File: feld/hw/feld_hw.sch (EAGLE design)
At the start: 23 parts, among them X1 PINH2X3N

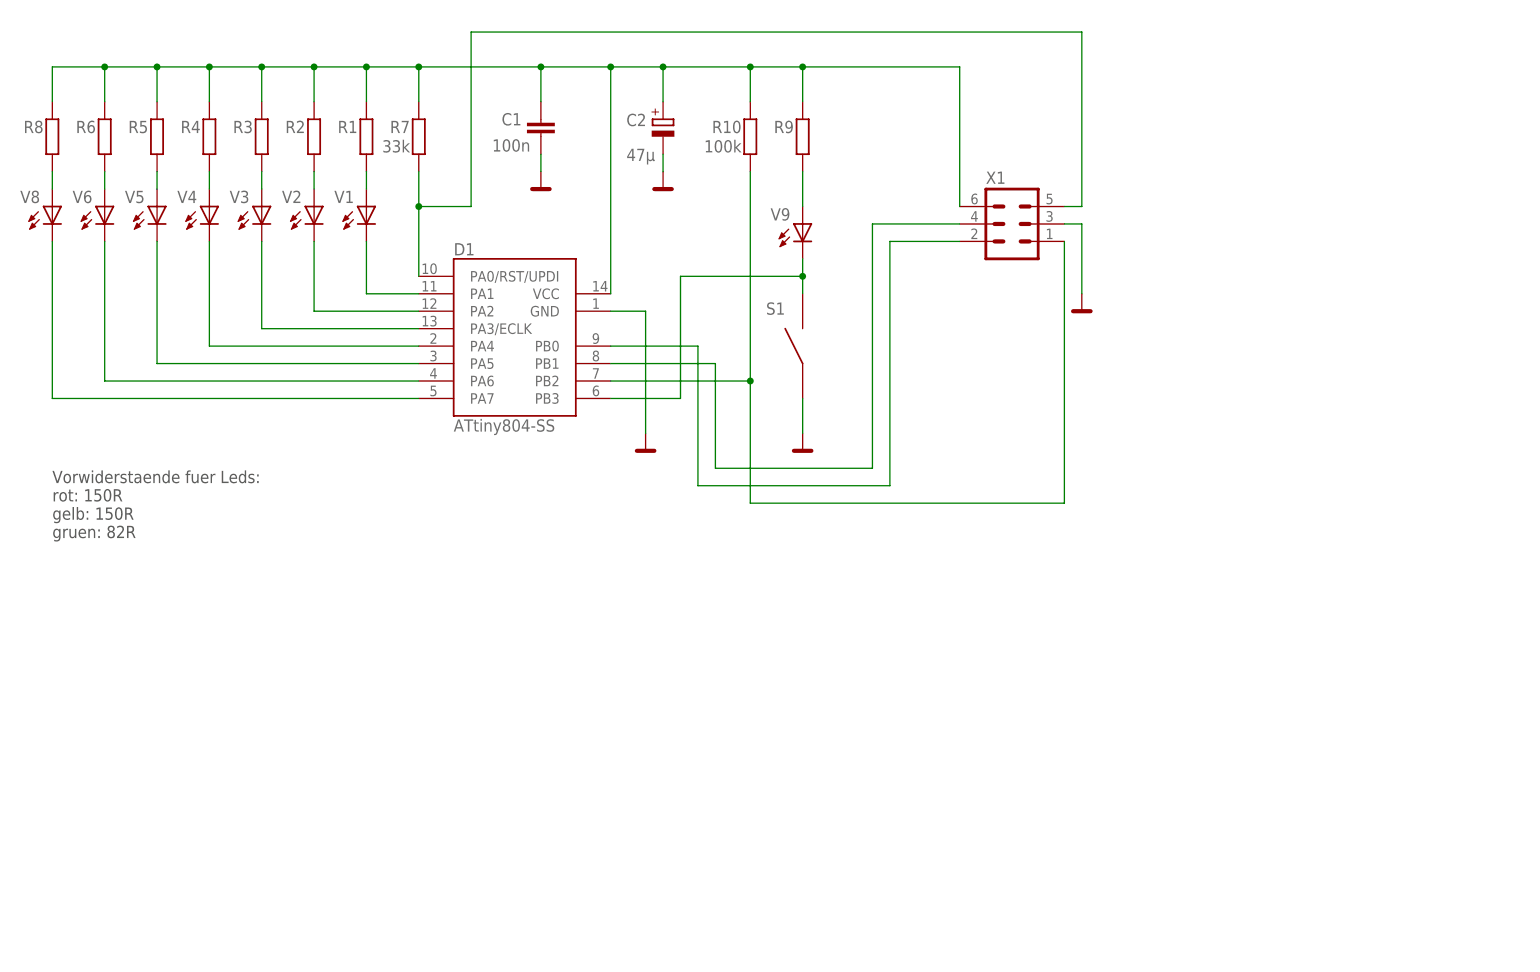
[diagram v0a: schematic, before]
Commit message: 
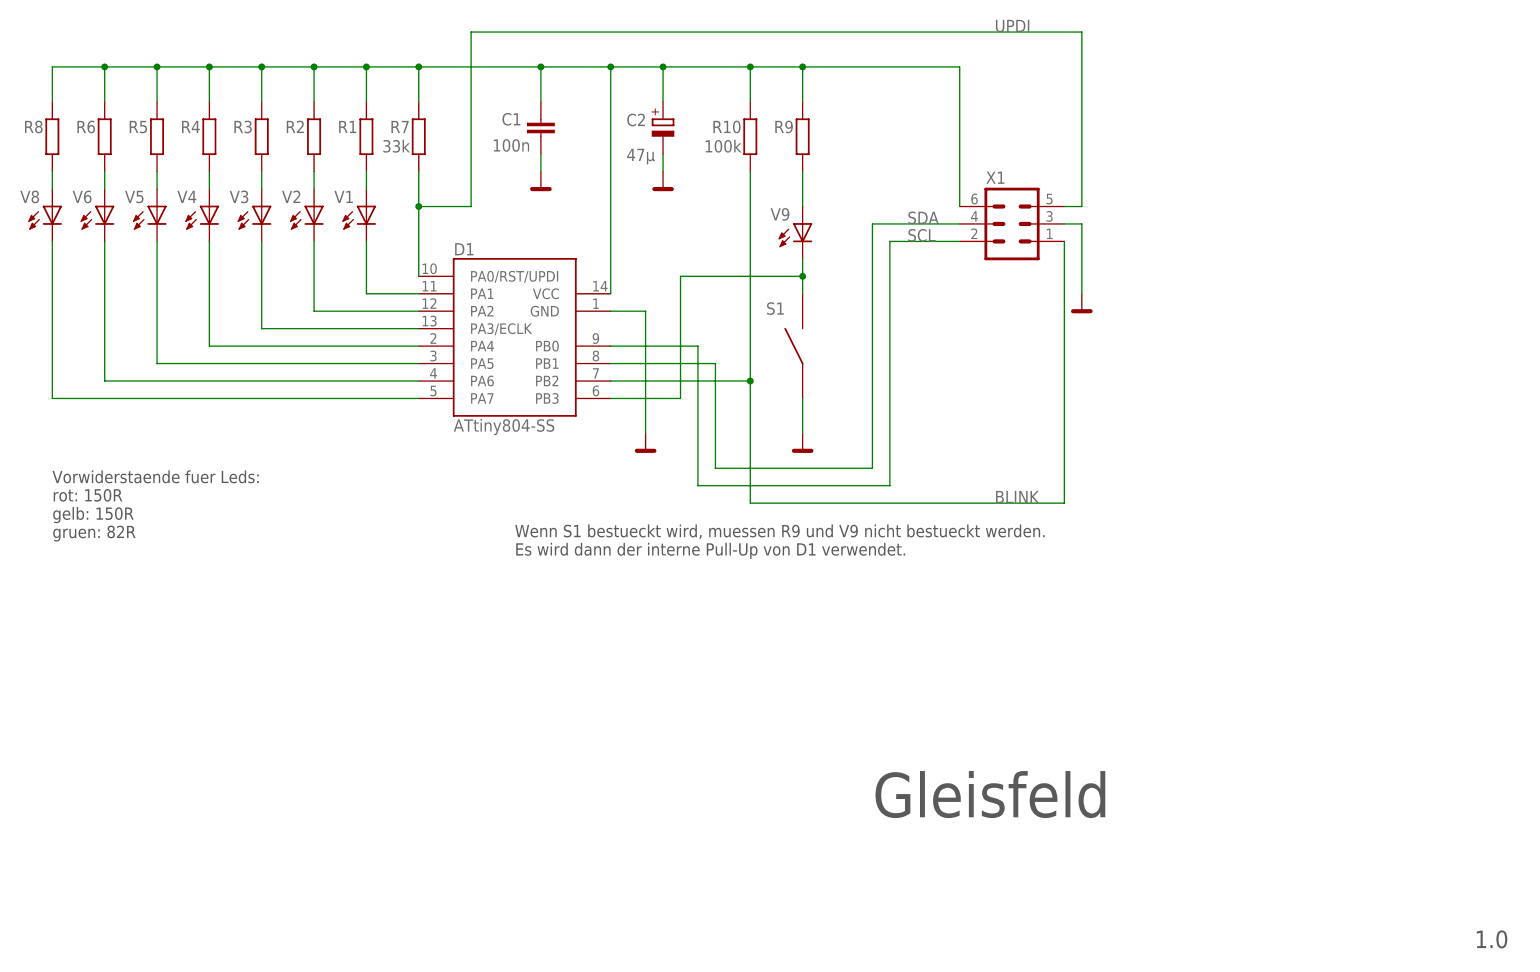
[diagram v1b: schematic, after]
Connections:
- net N$15 renamed UPDI
- net N$19 renamed SCL
- net N$20 renamed SDA
- net N$21 renamed BLINK
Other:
- note added: "1.0"
- note added: "Gleisfeld"
- note added: "Wenn S1 bestueckt wird, muessen R9 und V9 nicht bestueckt werden. Es wird dann der interne Pull-Up von D1 verwendet."
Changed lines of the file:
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@@
 gelb: 150R
 gruen: 82R</text>
+<text x="69.85" y="20.32" size="1.778" layer="97">Wenn S1 bestueckt wird, muessen R9 und V9 nicht bestueckt werden.
+Es wird dann der interne Pull-Up von D1 verwendet.</text>
+<text x="121.92" y="-17.78" size="6.4516" layer="97" font="vector">Gleisfeld</text>
+<text x="209.55" y="-36.83" size="2.54" layer="97">1.0</text>
 </plain>
 <instances>
@@
 </segment>
 </net>
-<net name="N$15" class="0">
+<net name="UPDI" class="0">
 <segment>
 <pinref part="D1" gate="G$1" pin="PA0/RST/UPDI"/>
@@
 <wire x1="63.5" y1="71.12" x2="55.88" y2="71.12" width="0.1524" layer="91"/>
 <junction x="55.88" y="71.12"/>
+<label x="139.7" y="96.52" size="1.778" layer="95"/>
 </segment>
 </net>
@@
 </segment>
 </net>
-<net name="N$19" class="0">
+<net name="SCL" class="0">
 <segment>
 <pinref part="D1" gate="G$1" pin="PB0"/>
@@
 <pinref part="X1" gate="G$1" pin="2"/>
 <wire x1="124.46" y1="66.04" x2="134.62" y2="66.04" width="0.1524" layer="91"/>
-</segment>
-</net>
-<net name="N$20" class="0">
+<label x="127" y="66.04" size="1.778" layer="95"/>
+</segment>
+</net>
+<net name="SDA" class="0">
 <segment>
 <pinref part="D1" gate="G$1" pin="PB1"/>
@@
 <pinref part="X1" gate="G$1" pin="4"/>
 <wire x1="121.92" y1="68.58" x2="134.62" y2="68.58" width="0.1524" layer="91"/>
-</segment>
-</net>
-<net name="N$21" class="0">
+<label x="127" y="68.58" size="1.778" layer="95"/>
+</segment>
+</net>
+<net name="BLINK" class="0">
 <segment>
 <pinref part="D1" gate="G$1" pin="PB2"/>
@@
 <wire x1="104.14" y1="27.94" x2="149.86" y2="27.94" width="0.1524" layer="91"/>
 <wire x1="149.86" y1="27.94" x2="149.86" y2="66.04" width="0.1524" layer="91"/>
-</segment>
-</net>
+<label x="139.7" y="27.94" size="1.778" layer="95"/>
+</segment>
+</net>
